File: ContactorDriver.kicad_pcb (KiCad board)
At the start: 2 copper layers, 38.5 x 52.9 mm, 43 parts, among them J1 PowerConn, J10 FanConn3, J11 FanConn4, J2 DashboardConnA, J3 ContactorAConn, J4 DashboardConnB, J5 ContactorBConn, J6 DashboardConnC, J7 ContactorCConn, J8 FanConn1, J9 FanConn2, Q1 PMV35EPER, Q2 IRLML0030TRPbF, Q3 IRLML0030TRPbF, Q4 IRLML0030TRPbF

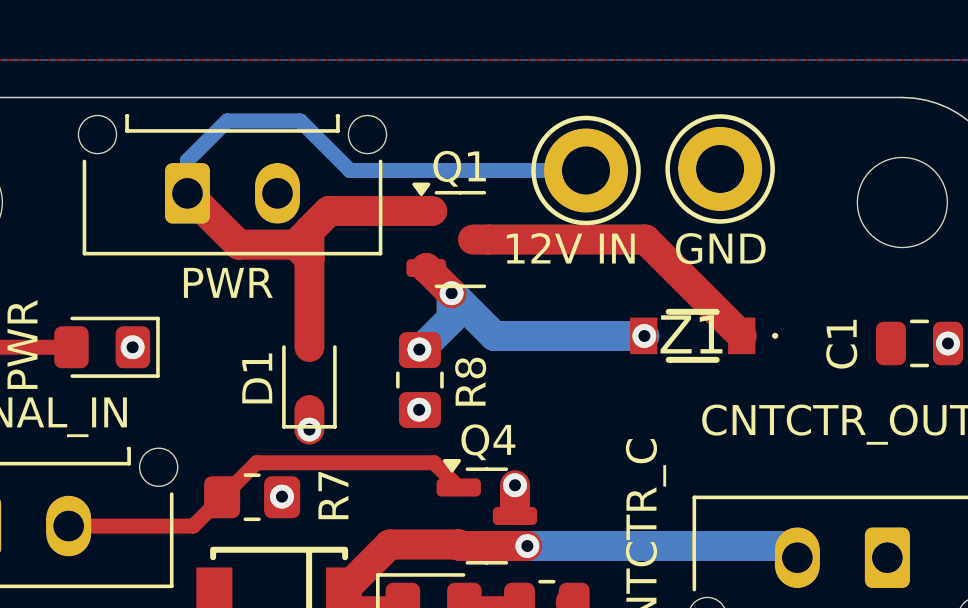
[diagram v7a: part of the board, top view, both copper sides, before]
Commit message: fixed the pmos pinout
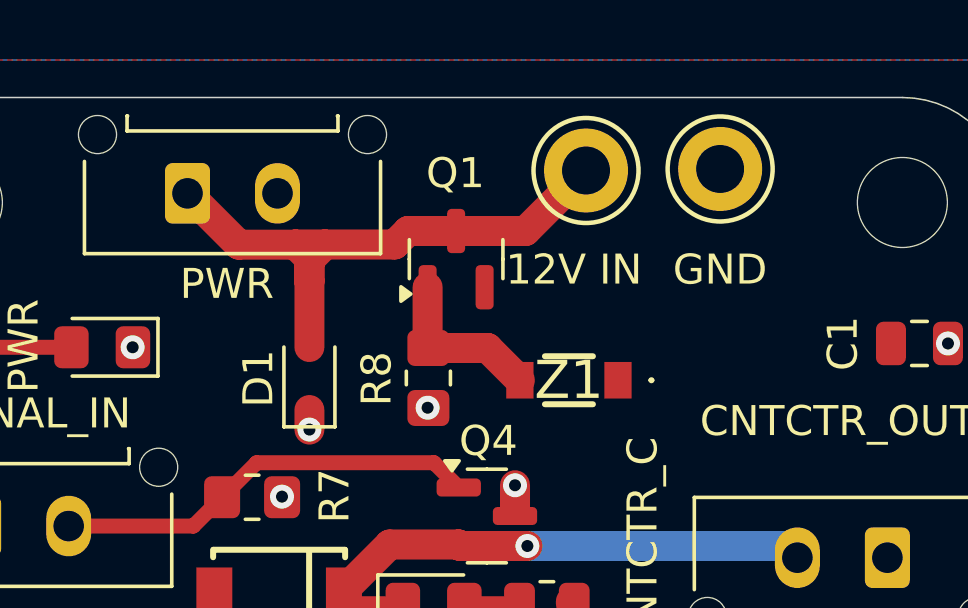
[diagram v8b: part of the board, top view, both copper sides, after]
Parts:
- Q1: footprint Package_TO_SOT_SMD:SOT-23-3 -> Package_TO_SOT_SMD:SOT-23
- moved Z1 4.38 mm to (147.2, 92.5)
- moved Q1 0.67 mm to (143.4, 88.5), turned to 90 degrees
- moved R8 0.29 mm to (142.5, 92.5)
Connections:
- Q1 pad 1: Net-(D1-A2) -> Net-(Q1-D)
- Q1 pad 2: Net-(Q1-G) -> +12V
- Q1 pad 3: +12V -> Net-(D1-A2)
- R8 pad 2: Net-(Q1-G) -> Net-(Q1-D)
- Z1 pad 2: Net-(Q1-G) -> Net-(Q1-D)
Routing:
- net Net-(Q1-G): track 10.6 -> 0.00 mm, vias 3 -> 0
- net Net-(D1-A2): track 30.4 -> 20.1 mm
- net +12V: track 11.6 -> 1.34 mm
- net Net-(Q1-D): track 0.00 -> 5.53 mm
